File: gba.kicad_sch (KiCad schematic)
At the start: 12 parts, among them IC1 STM32MP157AAB3, IC7 S40FC004C1B2C00000, SW1 SW_MEC_5G, SW2 SW_MEC_5G

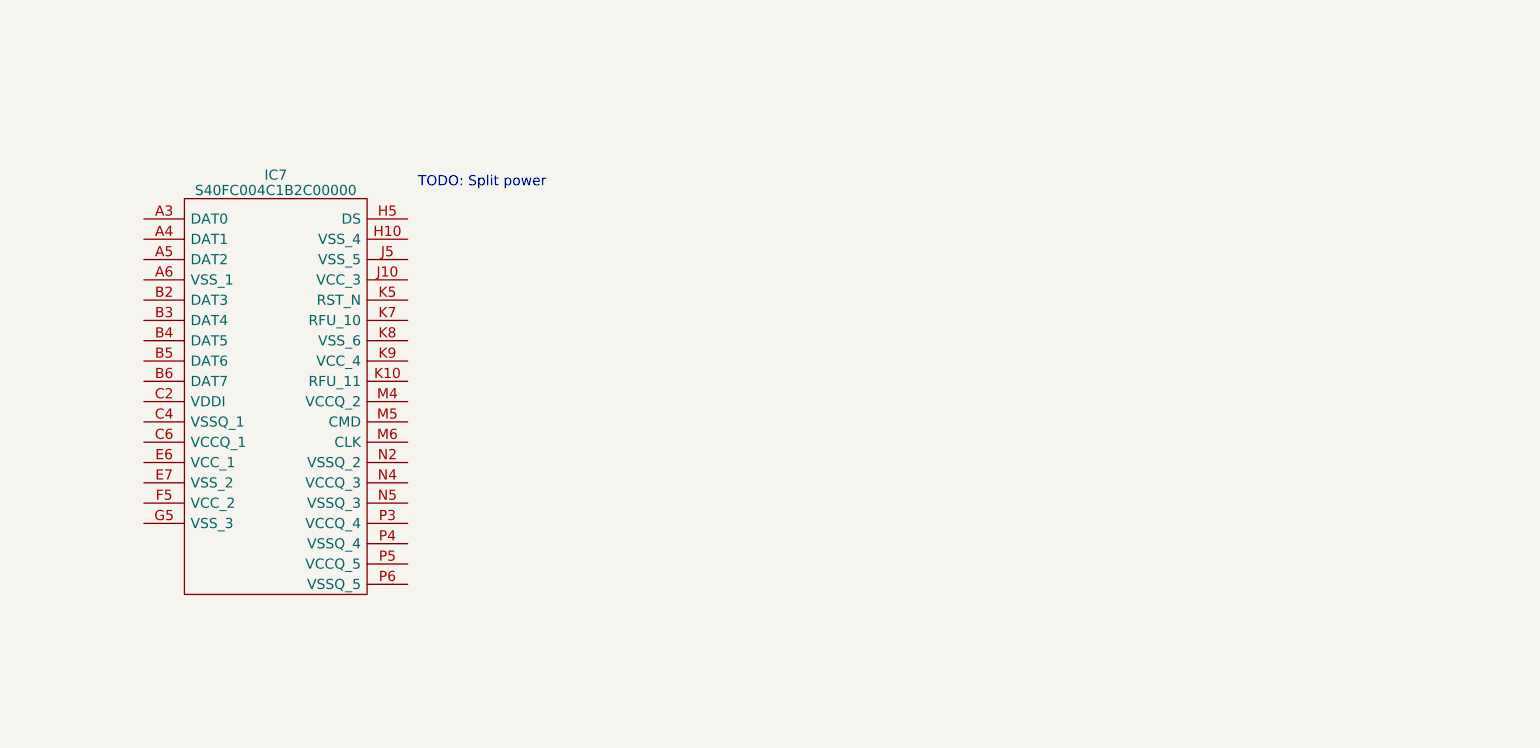
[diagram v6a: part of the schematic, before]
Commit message: Update eMMC Chip
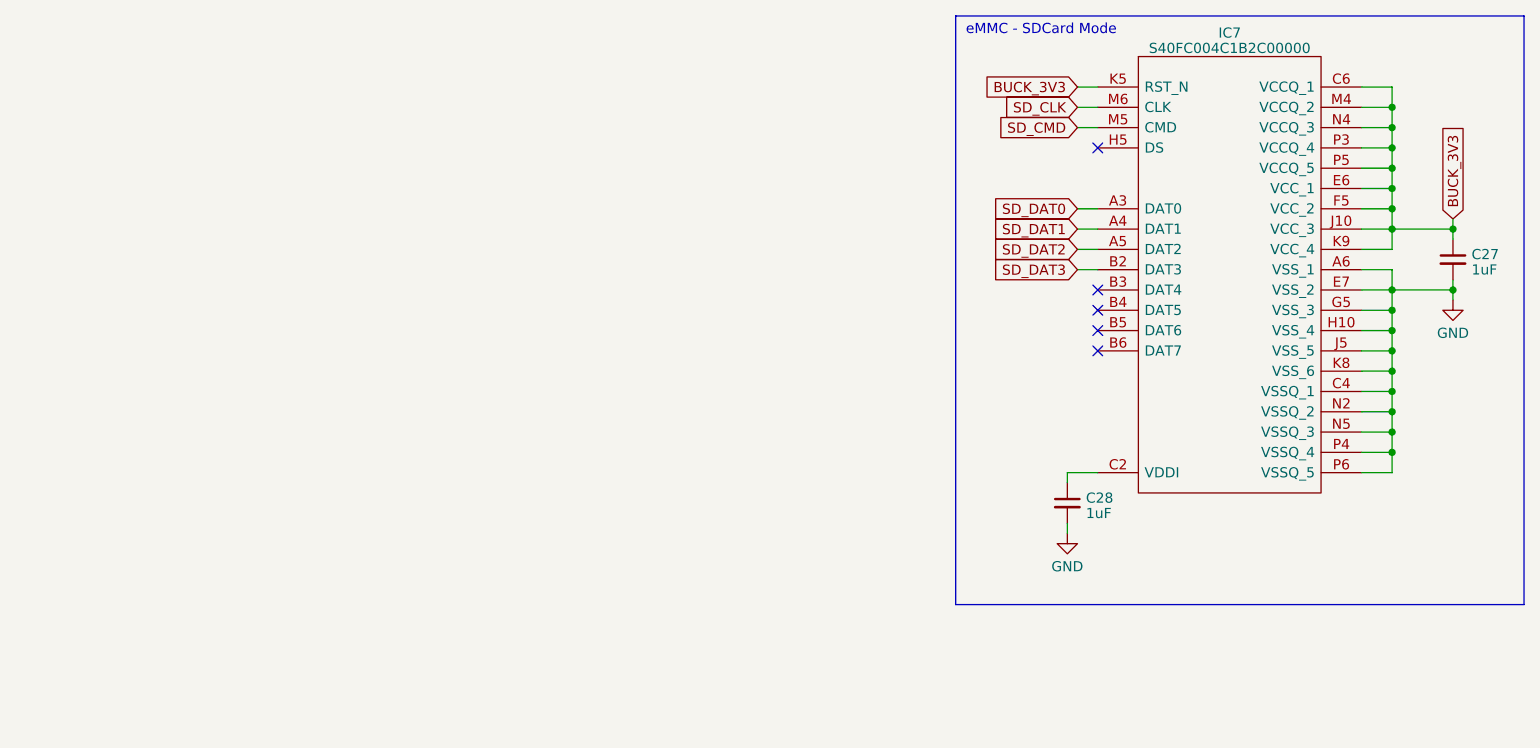
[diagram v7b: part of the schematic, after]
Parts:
- added C27, C28: 1uF, symbol Device:C_Small
- IC7: footprint BGA153C50P14X14_900X750X80 -> ARMband:BGA153C50P14X14_900X750X80
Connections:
- net BUCK_3V3: now also IC7.C6 (VCCQ_1), IC7.E6 (VCC_1), IC7.F5 (VCC_2), IC7.J10 (VCC_3), IC7.K5 (RST_N), IC7.K9 (VCC_4), IC7.M4 (VCCQ_2), IC7.N4 (VCCQ_3), IC7.P3 (VCCQ_4), IC7.P5 (VCCQ_5), C27.1
- net GND: now also IC7.A6 (VSS_1), IC7.C4 (VSSQ_1), IC7.E7 (VSS_2), IC7.G5 (VSS_3), IC7.H10 (VSS_4), IC7.J5 (VSS_5), IC7.K8 (VSS_6), IC7.N2 (VSSQ_2), IC7.N5 (VSSQ_3), IC7.P4 (VSSQ_4), IC7.P6 (VSSQ_5), C27.2, C28.2
- net SD_DAT0: now reaches IC7.A3 (DAT0)
- net SD_DAT1: now reaches IC7.A4 (DAT1)
- net SD_DAT2: now reaches IC7.A5 (DAT2)
- net SD_DAT3: now reaches IC7.B2 (DAT3)
- net at IC7.C2 (VDDI): now also C28.1
- net SD_CMD: now reaches IC7.M5 (CMD)
- net SD_CLK: now reaches IC7.M6 (CLK)
- no-connect marks 0 -> 5
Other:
- note added: "eMMC - SDCard Mode"
- note removed: "TODO: Split power"

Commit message: Added gas gauge and Li-Ion charging
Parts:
- added R11 (x2): 10k, Resistor_SMD:R_0603_1608Metric, symbol Device:R_Small
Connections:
- net BUCK_3V3: now also R11.1, R11.1
- net USB_D-: now reaches IC1.V13 (USB__DM2)
- net USB_D+: now reaches IC1.W13 (USB_DP2)
- new net SCL: R11.2
- new net SDA: R11.2
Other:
- note added: "I2C Pullups"
- note added: "NRST + opt buttons"
- moved on the sheet: C1, C2, C27, C28, IC7, R, R1, R2, R3, R4, R5, SW1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
